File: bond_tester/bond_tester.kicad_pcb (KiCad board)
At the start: 2 copper layers, 40 x 100 mm, 5 parts

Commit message: Rev bond_tester
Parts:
- moved G*** 27.1 mm to (108.8, 115.2)
- moved D 10.9 mm to (109.2, 110.0)
- moved C 8.19 mm to (109.2, 93.0)
- moved B 5.84 mm to (109.2, 76.0)
- moved A 4.37 mm to (109.2, 59.0)
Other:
- board size 40 x 100 mm -> 30 x 80 mm
- board text added: "Wirebond Tester C Fangmeier 2019"
- board text removed: "C Fangmeier 2019"
- board text removed: "Wirebond Tester"

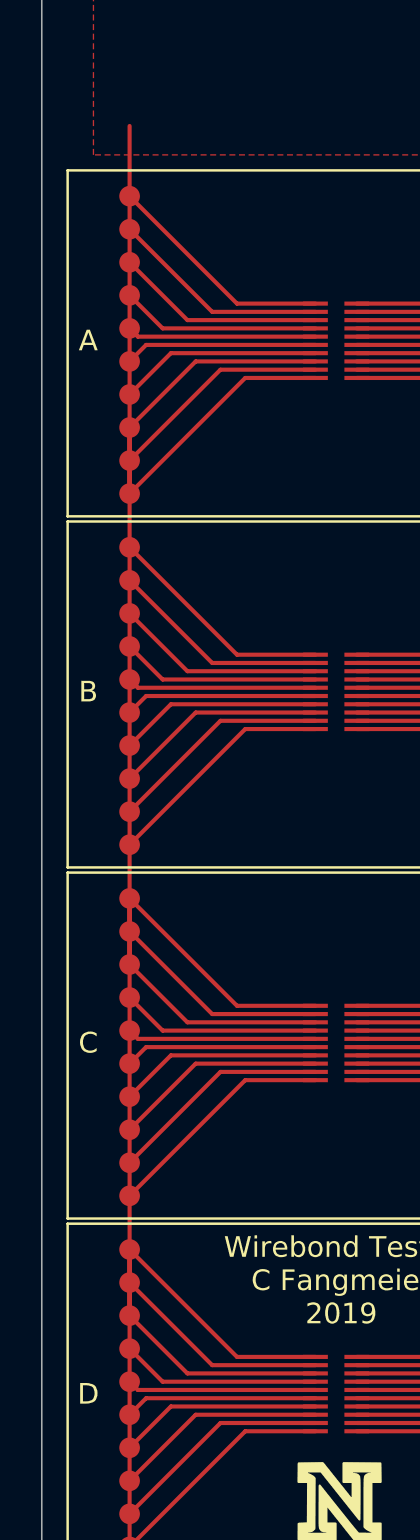
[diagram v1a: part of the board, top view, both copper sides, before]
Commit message: Fixes bond_tester schematic<-->board associations
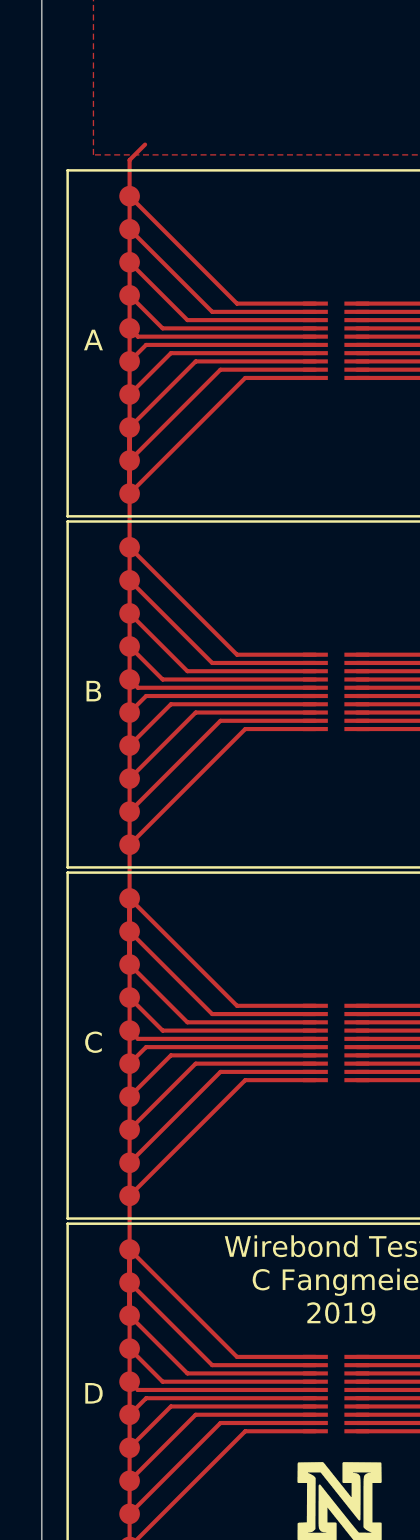
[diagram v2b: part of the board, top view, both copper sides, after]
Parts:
- removed B, C, D: Conn_02x10_Odd_Even, unl_silab:2x10_wirebond_pads_and_testpts
- added G2: Conn_02x10_Counter_Clockwise, unl_silab:2x10_wirebond_pads_and_testpts, F.Cu at (109.2, 76.0)
- added G3: Conn_02x10_Counter_Clockwise, unl_silab:2x10_wirebond_pads_and_testpts, F.Cu at (109.2, 93.0)
- added G4: Conn_02x10_Counter_Clockwise, unl_silab:2x10_wirebond_pads_and_testpts, F.Cu at (109.2, 110.0)
- G1: renamed from A; value Conn_02x10_Odd_Even -> Conn_02x10_Counter_Clockwise
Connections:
- G1 pad 1: (no net) -> /GND
- G1 pad 10: (no net) -> /GND
- G1 pad 11: (no net) -> Net-(G1-Pad11)
- G1 pad 12: (no net) -> Net-(G1-Pad12)
- G1 pad 13: (no net) -> Net-(G1-Pad13)
- G1 pad 14: (no net) -> Net-(G1-Pad14)
- G1 pad 15: (no net) -> Net-(G1-Pad15)
- G1 pad 16: (no net) -> Net-(G1-Pad16)
- G1 pad 17: (no net) -> Net-(G1-Pad17)
- G1 pad 18: (no net) -> Net-(G1-Pad18)
- G1 pad 19: (no net) -> Net-(G1-Pad19)
- G1 pad 2: (no net) -> /GND
- G1 pad 20: (no net) -> Net-(G1-Pad20)
- G1 pad 3: (no net) -> /GND
- G1 pad 4: (no net) -> /GND
- G1 pad 5: (no net) -> /GND
- G1 pad 6: (no net) -> /GND
- G1 pad 7: (no net) -> /GND
- G1 pad 8: (no net) -> /GND
- G1 pad 9: (no net) -> /GND
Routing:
- net (no net): track 897.2 -> 0.00 mm
- net /GND: track 0.00 -> 486.9 mm
- net Net-(G4-Pad20): track 0.00 -> 11.3 mm
- net Net-(G3-Pad20): track 0.00 -> 11.3 mm
- net Net-(G2-Pad20): track 0.00 -> 11.3 mm
- net Net-(G1-Pad20): track 0.00 -> 11.3 mm
- net Net-(G4-Pad11): track 0.00 -> 11.2 mm
- net Net-(G3-Pad11): track 0.00 -> 11.2 mm
- net Net-(G2-Pad11): track 0.00 -> 11.2 mm
- net Net-(G1-Pad11): track 0.00 -> 11.2 mm
- net Net-(G1-Pad19): track 0.00 -> 10.8 mm
- net Net-(G4-Pad19): track 0.00 -> 10.8 mm
- net Net-(G3-Pad19): track 0.00 -> 10.8 mm
- net Net-(G2-Pad19): track 0.00 -> 10.8 mm
- net Net-(G4-Pad12): track 0.00 -> 10.7 mm
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- added copper zone on F.Cu, net /GND
- removed copper zone on F.Cu, net (none)
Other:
- board text added: "A"
- board text added: "B"
- board text added: "C"
- board text added: "D"

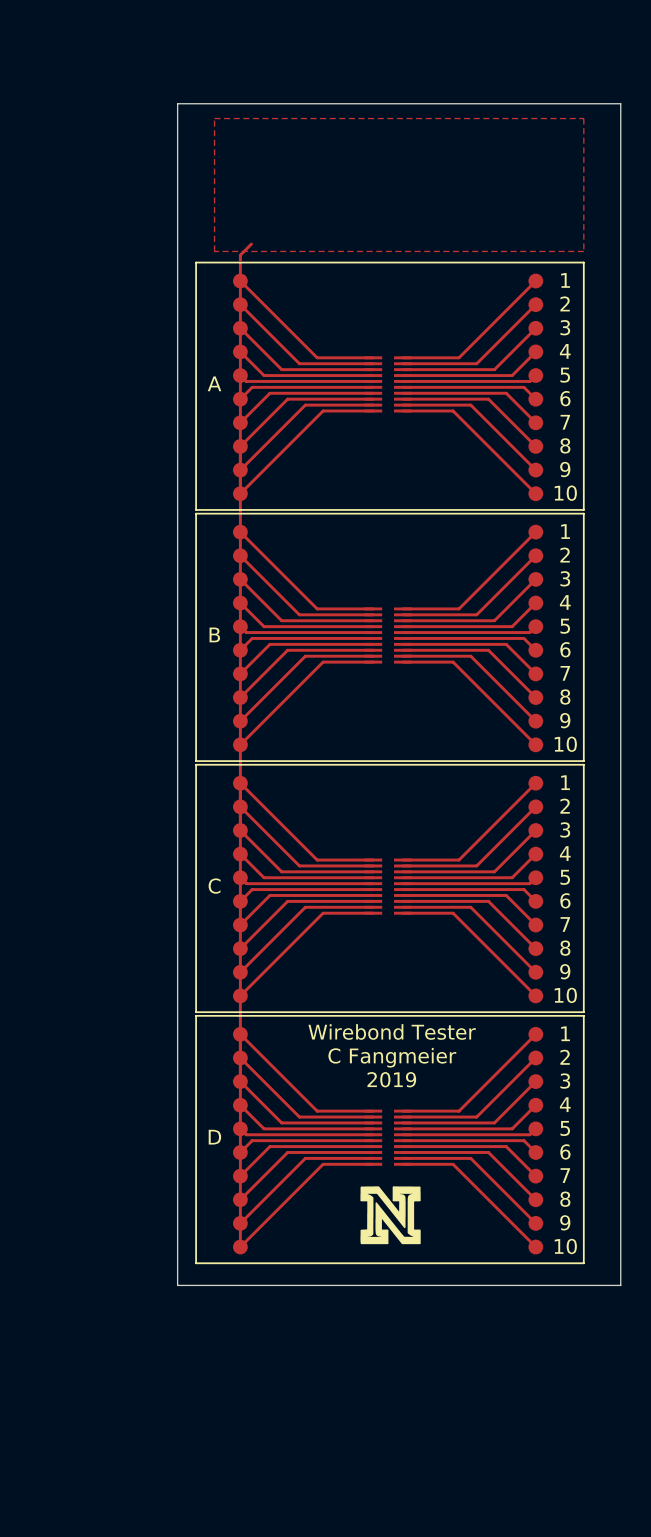
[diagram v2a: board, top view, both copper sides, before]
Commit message: Adds fiducial markings to bond_tester board
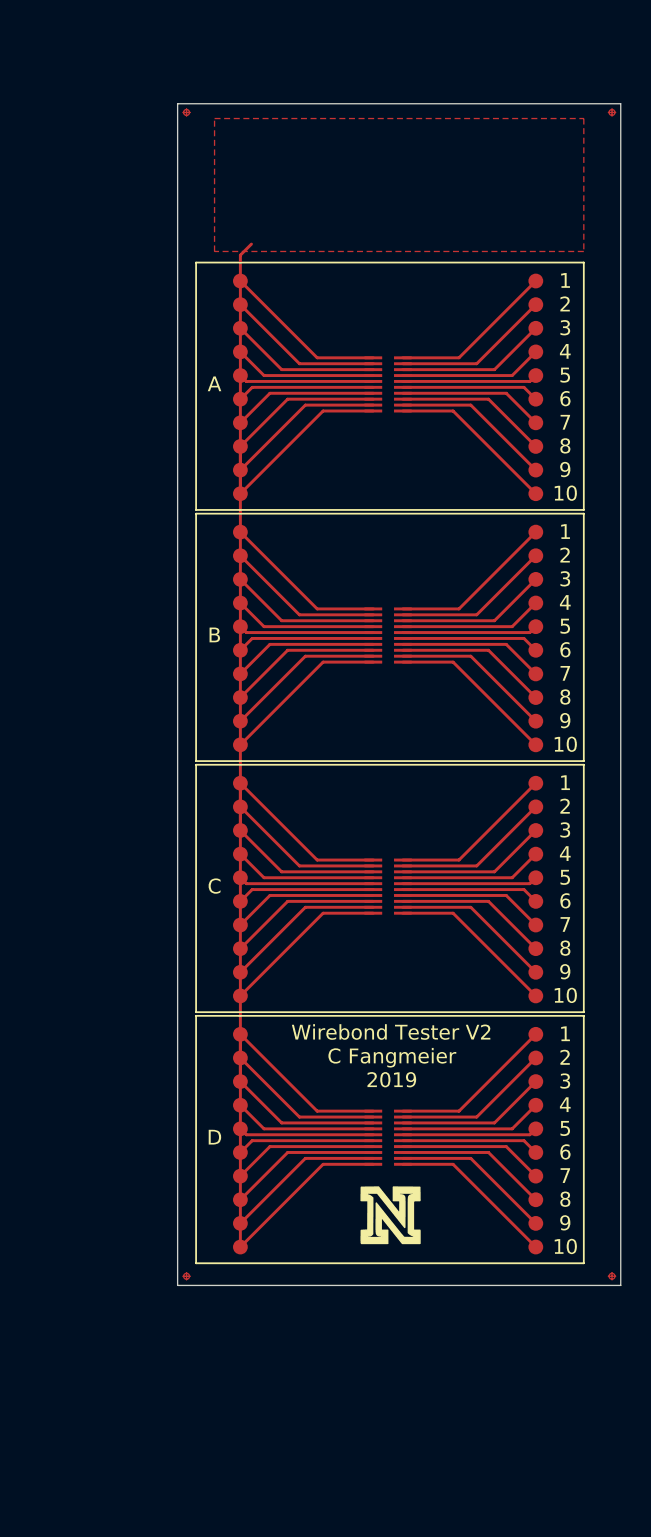
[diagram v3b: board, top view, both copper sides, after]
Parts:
- added REF**: crossed_circle_fiducial, unl_silab:crossed_circle_fiducial, F.Cu at (124.4, 119.4)
- added REF**: crossed_circle_fiducial, unl_silab:crossed_circle_fiducial, F.Cu at (95.6, 119.4)
- added REF**: crossed_circle_fiducial, unl_silab:crossed_circle_fiducial, F.Cu at (124.4, 40.6)
- added REF**: crossed_circle_fiducial, unl_silab:crossed_circle_fiducial, F.Cu at (95.6, 40.6)
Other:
- board text added: "Wirebond Tester V2 C Fangmeier 2019"
- board text removed: "Wirebond Tester C Fangmeier 2019"

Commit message: Updates bond_tester to version 2
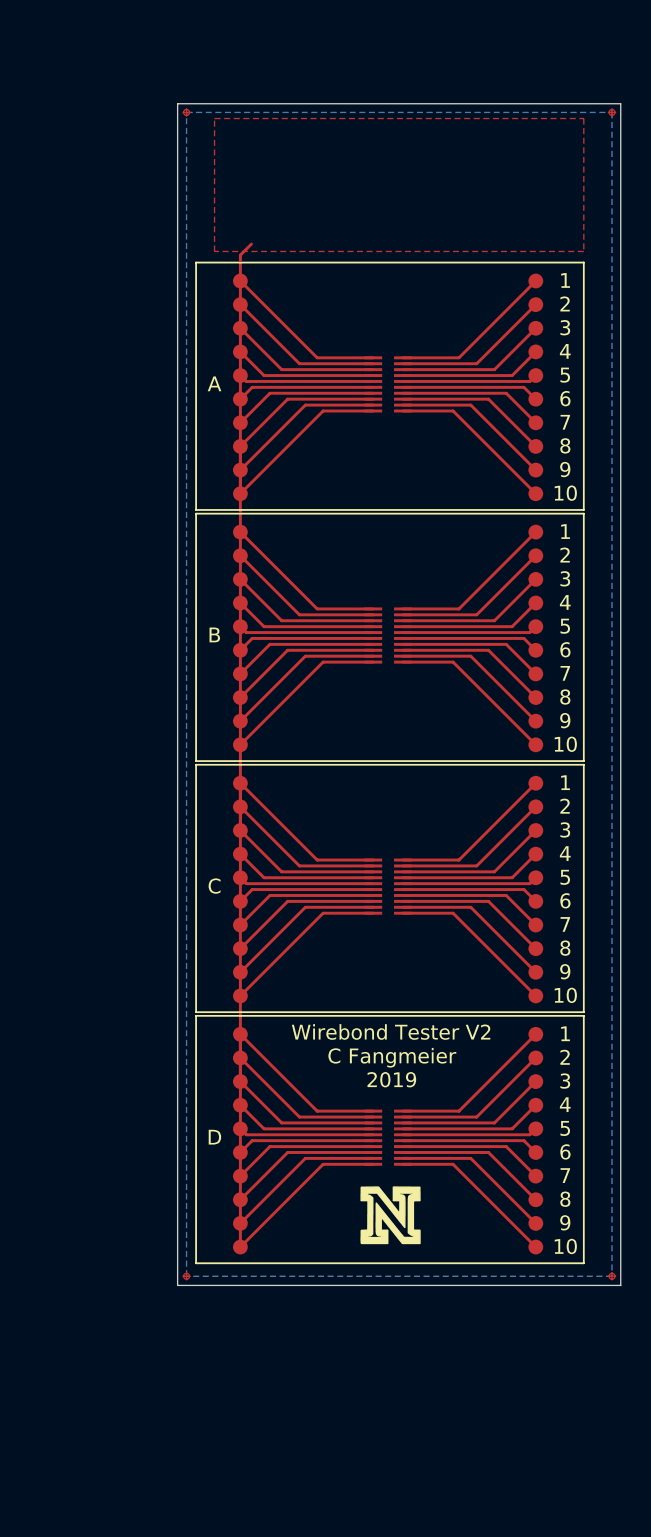
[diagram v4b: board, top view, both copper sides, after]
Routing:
- added copper zone on B.Cu, net (none)
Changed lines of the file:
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@@
     (visible_elements FFFFFF7F)
     (pcbplotparams
-      (layerselection 0x010fc_ffffffff)
-      (usegerberextensions false)
+      (layerselection 0x010e0_ffffffff)
+      (usegerberextensions true)
       (usegerberattributes false)
       (usegerberadvancedattributes false)
@@
       (outputformat 1)
       (mirror false)
-      (drillshape 1)
+      (drillshape 0)
       (scaleselection 1)
-      (outputdirectory ""))
+      (outputdirectory "gerbers/"))
   )
   (net 0 "")
@@
       )
     )
+  )
+  (zone (net 0) (net_name "") (layer B.Cu) (hatch edge 0.508)
+    (connect_pads (clearance 0.254))
+    (min_thickness 0.254)
+    (fill yes (arc_segments 32) (thermal_gap 0.508) (thermal_bridge_width 0.508))
+    (polygon
+      (pts
+        (xy 124.4092 119.38) (xy 95.6056 119.38) (xy 95.6056 40.5892) (xy 124.4092 40.5892)
+      )
+    )
